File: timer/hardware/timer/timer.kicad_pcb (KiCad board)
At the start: 2 copper layers, 115 x 78.4 mm, 22 parts, among them J1 Conn_02x05_Odd_Even, U1 74HC590, U2 74HC590, U3 74HC590, U4 74HC590, U5 74HC590, U6 74HC590, U7 74HC688, U8 74HC688, U9 ATF22V10C

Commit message: layout improvements
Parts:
- added R1: 22Ω, Resistor_THT:R_Axial_DIN0207_L6.3mm_D2.5mm_P10.16mm_Horizontal, F.Cu at (78.8, 89.0)
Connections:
- U1 pad 11: CLK -> ICLK
- U2 pad 11: CLK -> ICLK
- U3 pad 11: CLK -> ICLK
- U4 pad 11: CLK -> ICLK
- U5 pad 11: CLK -> ICLK
- U6 pad 11: CLK -> ICLK
- U9 pad 23: unconnected-(U9-I/O9-Pad23) -> Net-(U9-I/O9)
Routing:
- net CLK: track 171.8 -> 38.9 mm
- net GND: track 542.0 -> 663.7 mm, vias 186 -> 191
- net ICLK: track 0.00 -> 105.9 mm
- net Net-(U9-I/O9): track 0.00 -> 6.26 mm
- net ~{OE4}: track 77.7 -> 83.2 mm
- net /A0: track 50.3 -> 54.7 mm
- net ~{OE5}: track 90.0 -> 94.0 mm
- net ~{OE2}: track 47.8 -> 51.5 mm
- net LATCH: track 145.3 -> 146.9 mm
- net ~{RO}: track 58.7 -> 59.8 mm
- net ~{OE0}: track 36.8 -> 36.1 mm
- net ~{OE3}: track 68.5 -> 69.2 mm
- net /A1: track 58.5 -> 59.1 mm
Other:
- board text added: "v1.2 by Michael Kanmprath"
- board text removed: "v1.0 by Michael Kanmprath"

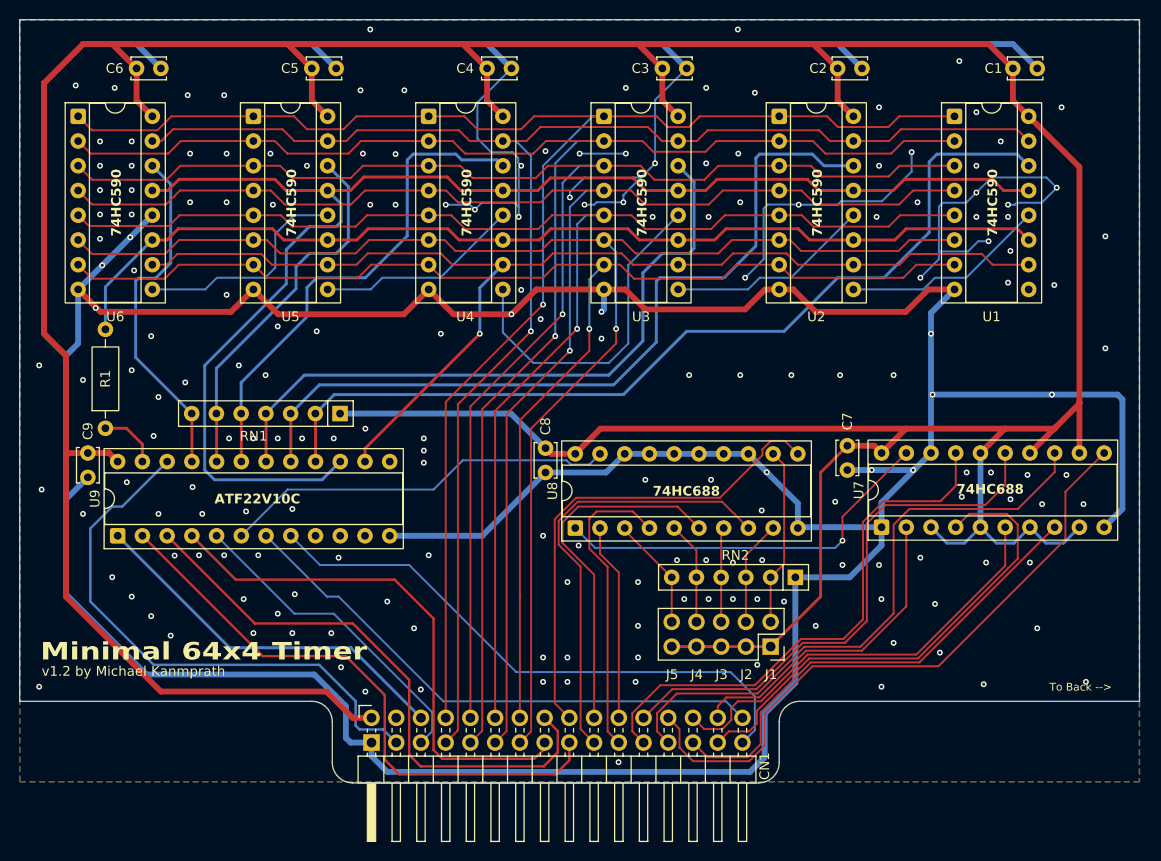
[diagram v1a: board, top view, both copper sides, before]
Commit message: corrected design flaw in hardware
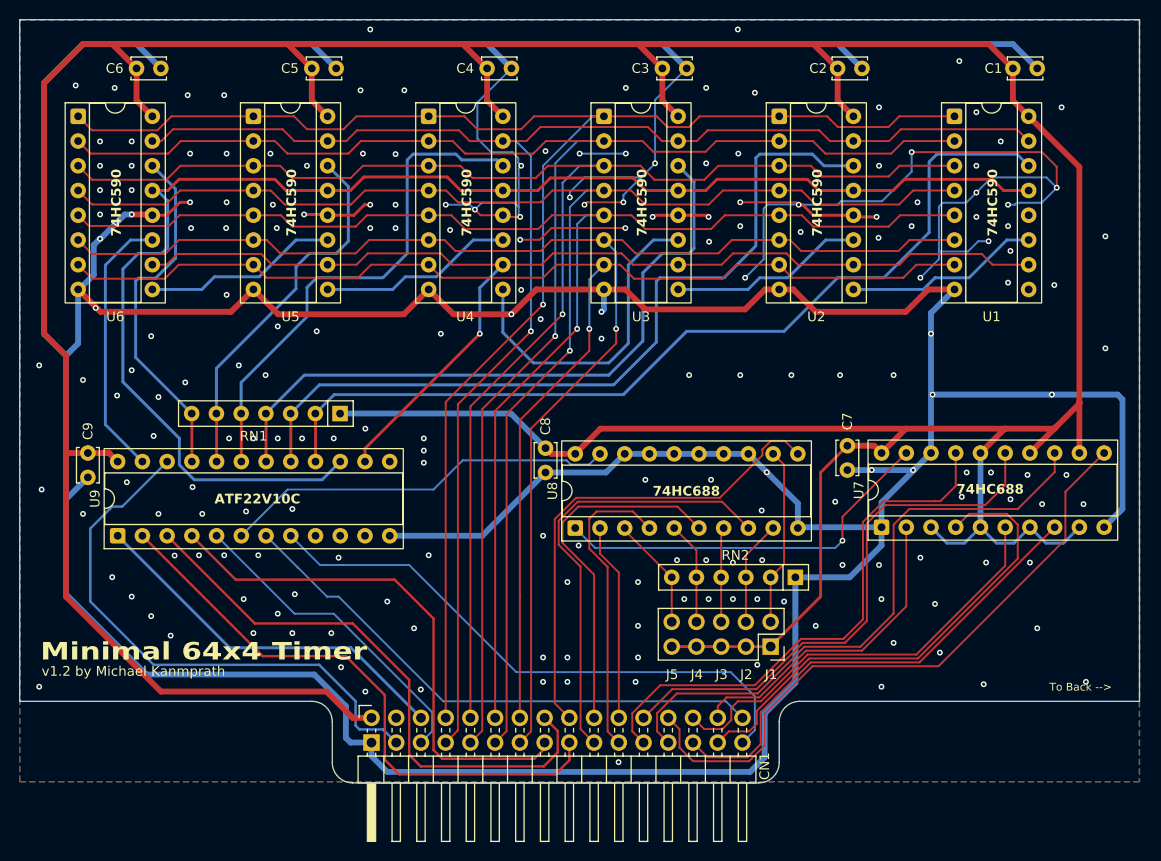
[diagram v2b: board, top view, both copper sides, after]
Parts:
- removed R1: 22Ω, Resistor_THT:R_Axial_DIN0207_L6.3mm_D2.5mm_P10.16mm_Horizontal
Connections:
- U1 pad 11: ICLK -> Net-(U1-CPC)
- U1 pad 12: Net-(U1-~{CE}) -> GND
- U2 pad 11: ICLK -> Net-(U2-CPC)
- U2 pad 12: Net-(U2-~{CE}) -> GND
- U2 pad 9: Net-(U1-~{CE}) -> Net-(U1-CPC)
- U3 pad 11: ICLK -> Net-(U3-CPC)
- U3 pad 12: Net-(U3-~{CE}) -> GND
- U3 pad 9: Net-(U2-~{CE}) -> Net-(U2-CPC)
- U4 pad 11: ICLK -> Net-(U4-CPC)
- U4 pad 12: Net-(U4-~{CE}) -> GND
- U4 pad 9: Net-(U3-~{CE}) -> Net-(U3-CPC)
- U5 pad 11: ICLK -> Net-(U5-CPC)
- U5 pad 12: Net-(U5-~{CE}) -> GND
- U5 pad 9: Net-(U4-~{CE}) -> Net-(U4-CPC)
- U6 pad 9: Net-(U5-~{CE}) -> Net-(U5-CPC)
- U9 pad 23: Net-(U9-I/O9) -> ICLK
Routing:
- net ICLK: track 105.9 -> 27.6 mm
- net GND: track 663.7 -> 731.7 mm, vias 191 -> 203
- net Net-(U3-~{CE}): track 34.7 -> 0.00 mm
- net Net-(U3-CPC): track 0.00 -> 33.7 mm
- net Net-(U5-~{CE}): track 23.2 -> 0.00 mm
- net Net-(U4-~{CE}): track 21.2 -> 0.00 mm
- net Net-(U1-~{CE}): track 21.2 -> 0.00 mm
- net Net-(U2-~{CE}): track 21.2 -> 0.00 mm
- net Net-(U2-CPC): track 0.00 -> 20.1 mm
- net Net-(U1-CPC): track 0.00 -> 20.1 mm
- net Net-(U5-CPC): track 0.00 -> 20.1 mm
- net Net-(U4-CPC): track 0.00 -> 20.1 mm
- net Net-(U9-I/O9): track 6.26 -> 0.00 mm
- net ~{OE2}: track 51.5 -> 52.6 mm
- net LATCH: track 146.9 -> 147.9 mm

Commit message: improved timer card design
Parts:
- removed RN1: 10K, Resistor_THT:R_Array_SIP7
- added U10: 74AHCT245, Package_DIP:DIP-20_W7.62mm_Socket, F.Cu at (111.6, 88.1)
- moved U9 3.60 mm to (76.5, 100.0)
- moved C9 3.60 mm to (73.4, 91.5)
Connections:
- U1 pad 1: /BUS1 -> /Q1
- U1 pad 15: /BUS0 -> /Q0
- U1 pad 2: /BUS2 -> /Q2
- U1 pad 3: /BUS3 -> /Q3
- U1 pad 4: /BUS4 -> /Q4
- U1 pad 5: /BUS5 -> /Q5
- U1 pad 6: /BUS6 -> /Q6
- U1 pad 7: /BUS7 -> /Q7
- U2 pad 1: /BUS1 -> /Q1
- U2 pad 15: /BUS0 -> /Q0
- U2 pad 2: /BUS2 -> /Q2
- U2 pad 3: /BUS3 -> /Q3
- U2 pad 4: /BUS4 -> /Q4
- U2 pad 5: /BUS5 -> /Q5
- U2 pad 6: /BUS6 -> /Q6
- U2 pad 7: /BUS7 -> /Q7
- U3 pad 1: /BUS1 -> /Q1
- U3 pad 15: /BUS0 -> /Q0
- U3 pad 2: /BUS2 -> /Q2
- U3 pad 3: /BUS3 -> /Q3
- U3 pad 4: /BUS4 -> /Q4
- U3 pad 5: /BUS5 -> /Q5
- U3 pad 6: /BUS6 -> /Q6
- U3 pad 7: /BUS7 -> /Q7
- U4 pad 1: /BUS1 -> /Q1
- U4 pad 15: /BUS0 -> /Q0
- U4 pad 2: /BUS2 -> /Q2
- U4 pad 3: /BUS3 -> /Q3
- U4 pad 4: /BUS4 -> /Q4
- U4 pad 5: /BUS5 -> /Q5
- U4 pad 6: /BUS6 -> /Q6
- U4 pad 7: /BUS7 -> /Q7
- U5 pad 1: /BUS1 -> /Q1
- U5 pad 15: /BUS0 -> /Q0
- U5 pad 2: /BUS2 -> /Q2
- U5 pad 3: /BUS3 -> /Q3
- U5 pad 4: /BUS4 -> /Q4
- U5 pad 5: /BUS5 -> /Q5
- U5 pad 6: /BUS6 -> /Q6
- U5 pad 7: /BUS7 -> /Q7
- U6 pad 1: /BUS1 -> /Q1
- U6 pad 15: /BUS0 -> /Q0
- U6 pad 2: /BUS2 -> /Q2
- U6 pad 3: /BUS3 -> /Q3
- U6 pad 4: /BUS4 -> /Q4
- U6 pad 5: /BUS5 -> /Q5
- U6 pad 6: /BUS6 -> /Q6
- U6 pad 7: /BUS7 -> /Q7
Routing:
- net /Q7: track 0.00 -> 145.4 mm, vias 0 -> 1
- net /Q4: track 0.00 -> 144.2 mm, vias 0 -> 1
- net /Q5: track 0.00 -> 144.1 mm, vias 0 -> 1
- net /Q3: track 0.00 -> 143.4 mm, vias 0 -> 1
- net /Q6: track 0.00 -> 143.2 mm, vias 0 -> 1
- net /Q2: track 0.00 -> 143.1 mm, vias 0 -> 1
- net /Q1: track 0.00 -> 141.8 mm, vias 0 -> 1
- net /BUS3: track 159.2 -> 19.1 mm, vias 1 -> 0
- net /BUS1: track 164.4 -> 25.3 mm, vias 1 -> 0
- net /BUS2: track 164.2 -> 25.2 mm, vias 1 -> 0
- net /BUS5: track 152.5 -> 13.9 mm, vias 1 -> 0
- net /BUS7: track 145.8 -> 8.65 mm, vias 1 -> 0
- net /BUS6: track 151.6 -> 14.6 mm, vias 1 -> 0
- net /Q0: track 0.00 -> 134.0 mm, vias 0 -> 1
- net /BUS4: track 158.1 -> 24.5 mm, vias 1 -> 0
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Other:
- board text added: "74HC245"
- board text added: "U10"
- board text added: "v1.3 by Michael Kanmprath"
- board text removed: "v1.2 by Michael Kanmprath"

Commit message: small tweaks
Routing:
- net ~{CLEAR}: track 150.8 -> 142.7 mm, vias 1 -> 0
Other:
- board text added: "v1.3.1 by Michael Kanmprath"
- board text removed: "v1.3 by Michael Kanmprath"
